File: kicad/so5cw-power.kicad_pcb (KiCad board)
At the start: 2 copper layers, 150 x 108 mm, 132 parts, among them J1 Screw_Terminal_01x02, J2 Screw_Terminal_01x02, J3 Screw_Terminal_01x02, J4 Screw_Terminal_01x02, J5 Screw_Terminal_01x02, J6 Raspberry Pi Zero 2W, J7 Screw_Terminal_01x02, J8 Screw_Terminal_01x02, J9 Screw_Terminal_01x02, K1 G2RL-1A-E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

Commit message: Connect Relay K2 to GPIO19, because GPIO1 is reserved
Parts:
- R43, R44, R45, R46, R47: value 10k -> 10
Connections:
- J6 pad 28: /K2G -> unconnected-(J6-ID_SC/GPIO1-Pad28)
- J6 pad 35: unconnected-(J6-GPIO19/MISO1-Pad35) -> /K2G
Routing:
- net /K2G: track 11.8 -> 22.3 mm
- net GND: vias 139 -> 142
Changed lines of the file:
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@@
 	(net 77 "unconnected-(U7-NC-Pad10)")
 	(net 78 "unconnected-(U7-IN6-Pad6)")
-	(net 79 "unconnected-(J6-GPIO19{slash}MISO1-Pad35)")
+	(net 79 "unconnected-(J6-ID_SC{slash}GPIO1-Pad28)")
 	(net 80 "/K2G")
 	(net 81 "unconnected-(J6-GPIO26-Pad37)")
@@
 			)
 		)
-		(property "Value" "10k"
+		(property "Value" "10"
 			(at 0 1.43 0)
 			(layer "F.Fab")
@@
 			)
 		)
-		(property "Value" "10k"
+		(property "Value" "10"
 			(at 0 1.43 0)
 			(layer "F.Fab")
@@
 			(layers "*.Cu" "*.Mask")
 			(remove_unused_layers no)
-			(net 80 "/K2G")
+			(net 79 "unconnected-(J6-ID_SC{slash}GPIO1-Pad28)")
 			(pinfunction "ID_SC/GPIO1")
 			(pintype "bidirectional")
@@
 			(layers "*.Cu" "*.Mask")
 			(remove_unused_layers no)
-			(net 79 "unconnected-(J6-GPIO19{slash}MISO1-Pad35)")
+			(net 80 "/K2G")
 			(pinfunction "GPIO19/MISO1")
 			(pintype "bidirectional")
@@
 			)
 		)
-		(property "Value" "10k"
+		(property "Value" "10"
 			(at 0 1.43 0)
 			(layer "F.Fab")
@@
 			)
 		)
-		(property "Value" "10k"
+		(property "Value" "10"
 			(at 0 1.43 0)
 			(layer "F.Fab")
@@
 			)
 		)
-		(property "Value" "10k"
+		(property "Value" "10"
 			(at 0 1.43 0)
 			(layer "F.Fab")
@@
 	)
 	(gr_rect
+		(start 160.725 133.035)
+		(end 167.655 137.025)
+		(stroke
+			(width 0.1)
+			(type solid)
+		)
+		(fill yes)
+		(layer "F.Mask")
+	)
+	(gr_rect
 		(start 66.84 36.76)
 		(end 216.84 144.76)
@@
 	)
 	(via
+		(at 201.49 86.91)
+		(size 0.8)
+		(drill 0.45)
+		(layers "F.Cu" "B.Cu")
+		(free yes)
+		(net 29)
+	)
+	(via
 		(at 70 50)
 		(size 0.8)
@@
 	)
 	(via
+		(at 201.49 90.91)
+		(size 0.8)
+		(drill 0.45)
+		(layers "F.Cu" "B.Cu")
+		(free yes)
+		(net 29)
+	)
+	(via
 		(at 86.15 65.76)
 		(size 0.8)
@@
 	)
 	(via
+		(at 201.49 95.91)
+		(size 0.8)
+		(drill 0.45)
+		(layers "F.Cu" "B.Cu")
+		(free yes)
+		(net 29)
+	)
+	(via
 		(at 200 140)
 		(size 0.8)
@@
 	)
 	(segment
-		(start 104.04 110.8725)
-		(end 104.04 106.02)
+		(start 97.06 113.72)
+		(end 99.0388 113.72)
 		(width 0.254)
 		(layer "F.Cu")
@@
 	)
 	(segment
-		(start 102.49 104.47)
-		(end 102.4888 104.47)
+		(start 103.739256 107.36)
+		(end 97.05 107.36)
 		(width 0.254)
 		(layer "F.Cu")
@@
 	)
 	(segment
-		(start 104.04 106.02)
-		(end 102.49 104.47)
+		(start 96.91 113.57)
+		(end 97.06 113.72)
 		(width 0.254)
 		(layer "F.Cu")
@@
 	)
 	(segment
-		(start 102.4888 104.47)
-		(end 101.5788 103.56)
+		(start 97.05 107.36)
+		(end 96.85 107.56)
 		(width 0.254)
 		(layer "F.Cu")
@@
 	(segment
 		(start 106.4675 113.3)
-		(end 104.04 110.8725)
+		(end 104.38 111.2125)
+		(width 0.254)
+		(layer "F.Cu")
+		(net 80)
+	)
+	(segment
+		(start 104.38 111.2125)
+		(end 104.38 108.000744)
+		(width 0.254)
+		(layer "F.Cu")
+		(net 80)
+	)
+	(segment
+		(start 96.85 107.56)
+		(end 96.85 113.57)
+		(width 0.254)
+		(layer "F.Cu")
+		(net 80)
+	)
+	(segment
+		(start 104.38 108.000744)
+		(end 103.739256 107.36)
+		(width 0.254)
+		(layer "F.Cu")
+		(net 80)
+	)
+	(segment
+		(start 96.85 113.57)
+		(end 96.91 113.57)
 		(width 0.254)
 		(layer "F.Cu")
@@
 	)
 	(segment
-		(start 102.98 108.64)
-		(end 101.5788 108.64)
+		(start 106.4675 116.35)
+		(end 103.74 113.6225)
 		(width 0.254)
 		(layer "F.Cu")
@@
 	)
 	(segment
-		(start 106.4675 116.35)
-		(end 103.08 112.9625)
+		(start 102.98 108.64)
+		(end 101.5788 108.64)
 		(width 0.254)
 		(layer "F.Cu")
@@
 	)
 	(segment
-		(start 103.08 112.9625)
-		(end 103.08 108.74)
+		(start 103.74 113.6225)
+		(end 103.74 109.4)
 		(width 0.254)
 		(layer "F.Cu")
@@
 	)
 	(segment
-		(start 103.08 108.74)
+		(start 103.74 109.4)
 		(end 102.98 108.64)
 		(width 0.254)

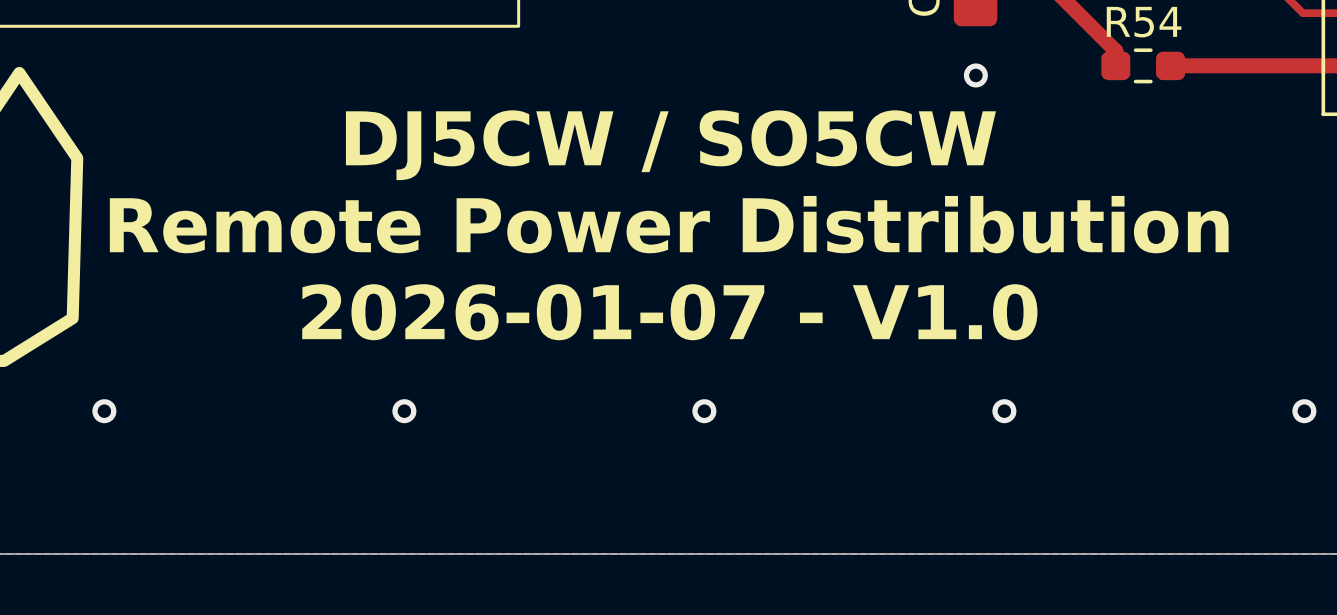
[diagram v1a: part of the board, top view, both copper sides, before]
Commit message: Version 1.1 (K2 re-routed from GPIO1 to GPIO19). Cosmetics.
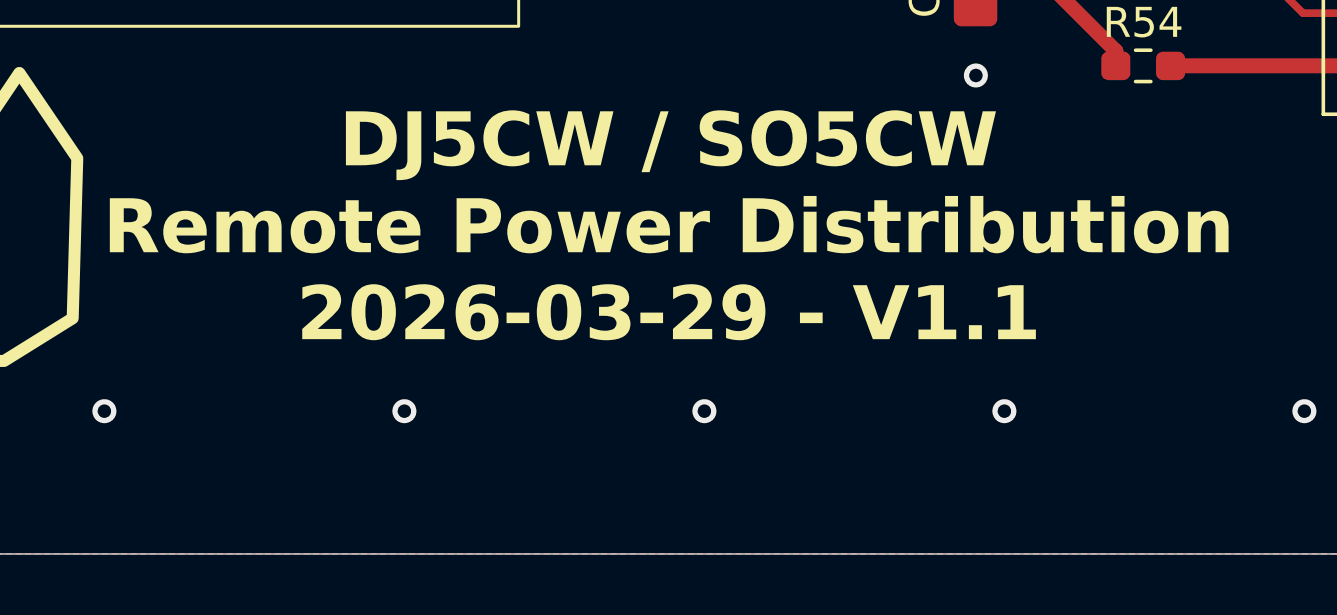
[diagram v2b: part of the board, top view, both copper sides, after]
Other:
- board text added: "DJ5CW / SO5CW Remote Power Distribution 2026-03-29 - V1.1"
- board text removed: "DJ5CW / SO5CW Remote Power Distribution 2026-01-07 - V1.0"
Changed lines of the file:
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@@
 		(layer "Edge.Cuts")
+	)
+	(gr_text "SCL"
+		(at 113.42 79.29 0)
+		(layer "F.SilkS")
+		(effects
+			(font
+				(size 1 1)
+				(thickness 0.15)
+			)
+			(justify left bottom)
+		)
+	)
+	(gr_text "SDA"
+		(at 113.52 73.22 0)
+		(layer "F.SilkS")
+		(effects
+			(font
+				(size 1 1)
+				(thickness 0.15)
+			)
+			(justify left bottom)
+		)
+	)
+	(gr_text "DC IN"
+		(at 180.17 139.31 0)
+		(layer "F.SilkS")
+		(effects
+			(font
+				(size 1 1)
+				(thickness 0.15)
+			)
+			(justify left bottom)
+		)
+	)
+	(gr_text "IN1"
+		(at 78.16 40.08 0)
+		(layer "F.SilkS")
+		(effects
+			(font
+				(size 1.1 1.1)
+				(thickness 0.24)
+				(bold yes)
+			)
+			(justify bottom)
+		)
+	)
+	(gr_text "IN2"
+		(at 91.57 40.08 0)
+		(layer "F.SilkS")
+		(effects
+			(font
+				(size 1.1 1.1)
+				(thickness 0.24)
+				(bold yes)
+			)
+			(justify bottom)
+		)
+	)
+	(gr_text "Protection active"
+		(at 111.29 47.33 0)
+		(layer "F.SilkS")
+		(effects
+			(font
+				(size 1.1 1.1)
+				(thickness 0.24)
+				(bold yes)
+			)
+			(justify bottom)
+		)
+	)
+	(gr_text "+"
+		(at 131.15 41.28 0)
+		(layer "F.SilkS")
+		(effects
+			(font
+				(size 1.1 1.1)
+				(thickness 0.24)
+				(bold yes)
+			)
+			(justify bottom)
+		)
+	)
+	(gr_text "OUT1: 13.8V"
+		(at 136.42 40.08 0)
+		(layer "F.SilkS")
+		(effects
+			(font
+				(size 1.1 1.1)
+				(thickness 0.24)
+				(bold yes)
+			)
+			(justify bottom)
+		)
+	)
+	(gr_text "-"
+		(at 141.48 41.49 0)
+		(layer "F.SilkS")
+		(effects
+			(font
+				(size 1.1 1.1)
+				(thickness 0.24)
+				(bold yes)
+			)
+			(justify bottom)
+		)
+	)
+	(gr_text "+"
+		(at 147.03 41.4 0)
+		(layer "F.SilkS")
+		(effects
+			(font
+				(size 1.1 1.1)
+				(thickness 0.24)
+				(bold yes)
+			)
+			(justify bottom)
+		)
 	)
 	(gr_text "OUT2: 13.8V"
@@
 	)
 	(gr_text "+"
+		(at 162.92 41.51 0)
+		(layer "F.SilkS")
+		(effects
+			(font
+				(size 1.1 1.1)
+				(thickness 0.24)
+				(bold yes)
+			)
+			(justify bottom)
+		)
+	)
+	(gr_text "OUT3: 5V"
+		(at 167.82 40.29 0)
+		(layer "F.SilkS")
+		(effects
+			(font
+				(size 1.1 1.1)
+				(thickness 0.24)
+				(bold yes)
+			)
+			(justify bottom)
+		)
+	)
+	(gr_text "-"
+		(at 173.33 41.39 0)
+		(layer "F.SilkS")
+		(effects
+			(font
+				(size 1.1 1.1)
+				(thickness 0.24)
+				(bold yes)
+			)
+			(justify bottom)
+		)
+	)
+	(gr_text "+"
+		(at 178.87 41.57 0)
+		(layer "F.SilkS")
+		(effects
+			(font
+				(size 1.1 1.1)
+				(thickness 0.24)
+				(bold yes)
+			)
+			(justify bottom)
+		)
+	)
+	(gr_text "OUT4: 13.8V"
+		(at 183.78 40.14 0)
+		(layer "F.SilkS")
+		(effects
+			(font
+				(size 1.1 1.1)
+				(thickness 0.24)
+				(bold yes)
+			)
+			(justify bottom)
+		)
+	)
+	(gr_text "-"
+		(at 189.24 41.52 0)
+		(layer "F.SilkS")
+		(effects
+			(font
+				(size 1.1 1.1)
+				(thickness 0.24)
+				(bold yes)
+			)
+			(justify bottom)
+		)
+	)
+	(gr_text "+"
 		(at 194.66 41.6 0)
 		(layer "F.SilkS")
@@
 		)
 	)
-	(gr_text "IN1"
-		(at 78.16 40.08 0)
-		(layer "F.SilkS")
-		(effects
-			(font
-				(size 1.1 1.1)
-				(thickness 0.24)
-				(bold yes)
-			)
-			(justify bottom)
-		)
-	)
-	(gr_text "+"
-		(at 147.03 41.4 0)
+	(gr_text "OUT5: 13.8V"
+		(at 199.64 40.14 0)
 		(layer "F.SilkS")
 		(effects
@@
 	(gr_text "-"
 		(at 205.06 41.52 0)
-		(layer "F.SilkS")
-		(effects
-			(font
-				(size 1.1 1.1)
-				(thickness 0.24)
-				(bold yes)
-			)
-			(justify bottom)
-		)
-	)
-	(gr_text "Protection active"
-		(at 111.29 47.33 0)
-		(layer "F.SilkS")
-		(effects
-			(font
-				(size 1.1 1.1)
-				(thickness 0.24)
-				(bold yes)
-			)
-			(justify bottom)
-		)
-	)
-	(gr_text "SCL"
-		(at 113.42 79.29 0)
-		(layer "F.SilkS")
-		(effects
-			(font
-				(size 1 1)
-				(thickness 0.15)
-			)
-			(justify left bottom)
-		)
-	)
-	(gr_text "-"
-		(at 173.33 41.39 0)
 		(layer "F.SilkS")
 		(effects
@@
 		)
 	)
-	(gr_text "OUT4: 13.8V"
-		(at 183.78 40.14 0)
-		(layer "F.SilkS")
-		(effects
-			(font
-				(size 1.1 1.1)
-				(thickness 0.24)
-				(bold yes)
-			)
-			(justify bottom)
-		)
-	)
-	(gr_text "DC IN"
-		(at 180.17 139.31 0)
-		(layer "F.SilkS")
-		(effects
-			(font
-				(size 1 1)
-				(thickness 0.15)
-			)
-			(justify left bottom)
-		)
-	)
-	(gr_text "IN2"
-		(at 91.57 40.08 0)
-		(layer "F.SilkS")
-		(effects
-			(font
-				(size 1.1 1.1)
-				(thickness 0.24)
-				(bold yes)
-			)
-			(justify bottom)
-		)
-	)
-	(gr_text "SDA"
-		(at 113.52 73.22 0)
-		(layer "F.SilkS")
-		(effects
-			(font
-				(size 1 1)
-				(thickness 0.15)
-			)
-			(justify left bottom)
-		)
-	)
-	(gr_text "OUT3: 5V"
-		(at 167.82 40.29 0)
-		(layer "F.SilkS")
-		(effects
-			(font
-				(size 1.1 1.1)
-				(thickness 0.24)
-				(bold yes)
-			)
-			(justify bottom)
-		)
-	)
-	(gr_text "DJ5CW / SO5CW\nRemote Power Distribution\n2026-01-07 - V1.0"
+	(gr_text "DJ5CW / SO5CW\nRemote Power Distribution\n2026-03-29 - V1.1"
 		(at 108.81 137.82 0)
 		(layer "F.SilkS")
@@
 				(bold yes)
 			)
-			(justify bottom)
-		)
-	)
-	(gr_text "+"
-		(at 131.15 41.28 0)
-		(layer "F.SilkS")
-		(effects
-			(font
-				(size 1.1 1.1)
-				(thickness 0.24)
-				(bold yes)
-			)
-			(justify bottom)
-		)
-	)
-	(gr_text "OUT5: 13.8V"
-		(at 199.64 40.14 0)
-		(layer "F.SilkS")
-		(effects
-			(font
-				(size 1.1 1.1)
-				(thickness 0.24)
-				(bold yes)
-			)
-			(justify bottom)
-		)
-	)
-	(gr_text "+"
-		(at 178.87 41.57 0)
-		(layer "F.SilkS")
-		(effects
-			(font
-				(size 1.1 1.1)
-				(thickness 0.24)
-				(bold yes)
-			)
-			(justify bottom)
-		)
-	)
-	(gr_text "OUT1: 13.8V"
-		(at 136.42 40.08 0)
-		(layer "F.SilkS")
-		(effects
-			(font
-				(size 1.1 1.1)
-				(thickness 0.24)
-				(bold yes)
-			)
-			(justify bottom)
-		)
-	)
-	(gr_text "+"
-		(at 162.92 41.51 0)
-		(layer "F.SilkS")
-		(effects
-			(font
-				(size 1.1 1.1)
-				(thickness 0.24)
-				(bold yes)
-			)
-			(justify bottom)
-		)
-	)
-	(gr_text "-"
-		(at 189.24 41.52 0)
-		(layer "F.SilkS")
-		(effects
-			(font
-				(size 1.1 1.1)
-				(thickness 0.24)
-				(bold yes)
-			)
-			(justify bottom)
-		)
-	)
-	(gr_text "-"
-		(at 141.48 41.49 0)
-		(layer "F.SilkS")
-		(effects
-			(font
-				(size 1.1 1.1)
-				(thickness 0.24)
-				(bold yes)
-			)
